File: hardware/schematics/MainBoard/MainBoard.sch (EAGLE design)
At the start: 16 parts, among them J1 T2M-105-01-X-D-TH-WT

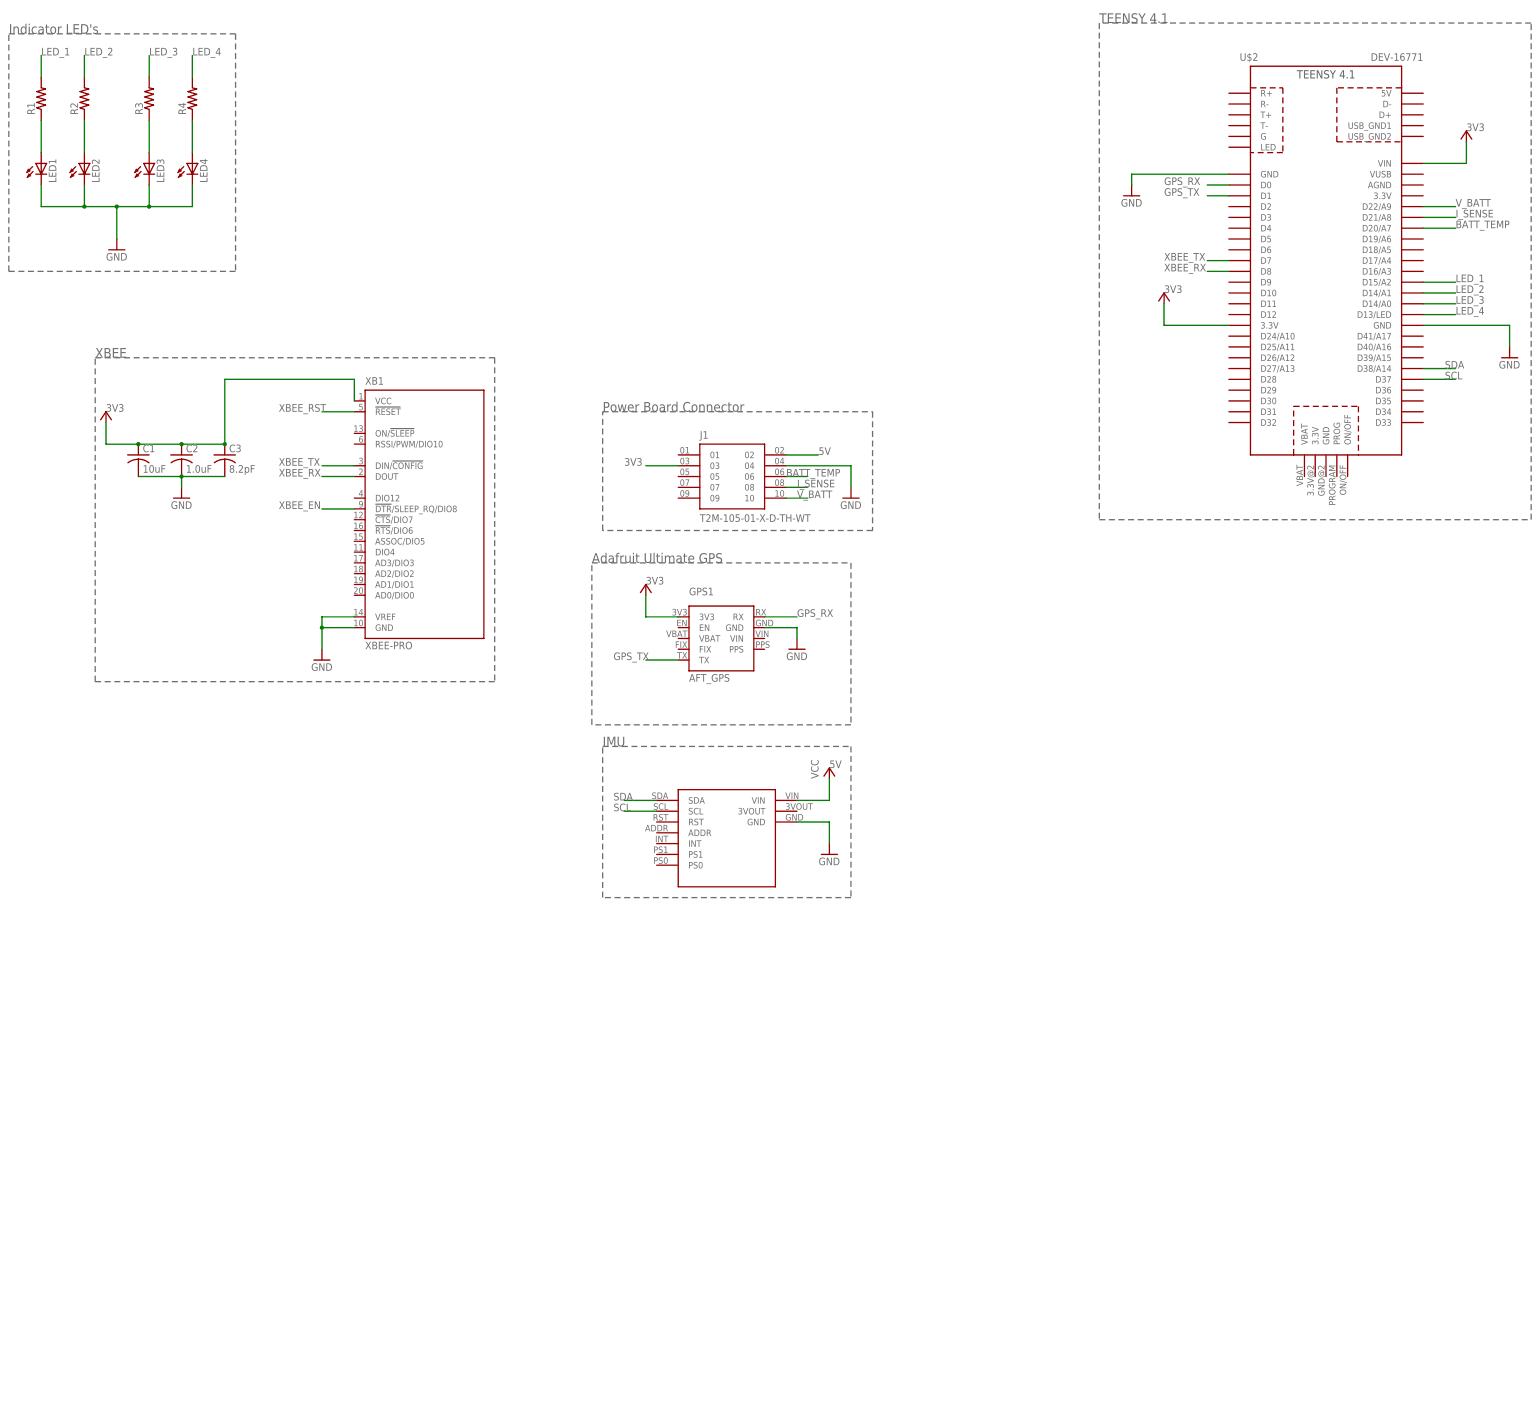
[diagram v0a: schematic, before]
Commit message: Added BMP388 & PDF's
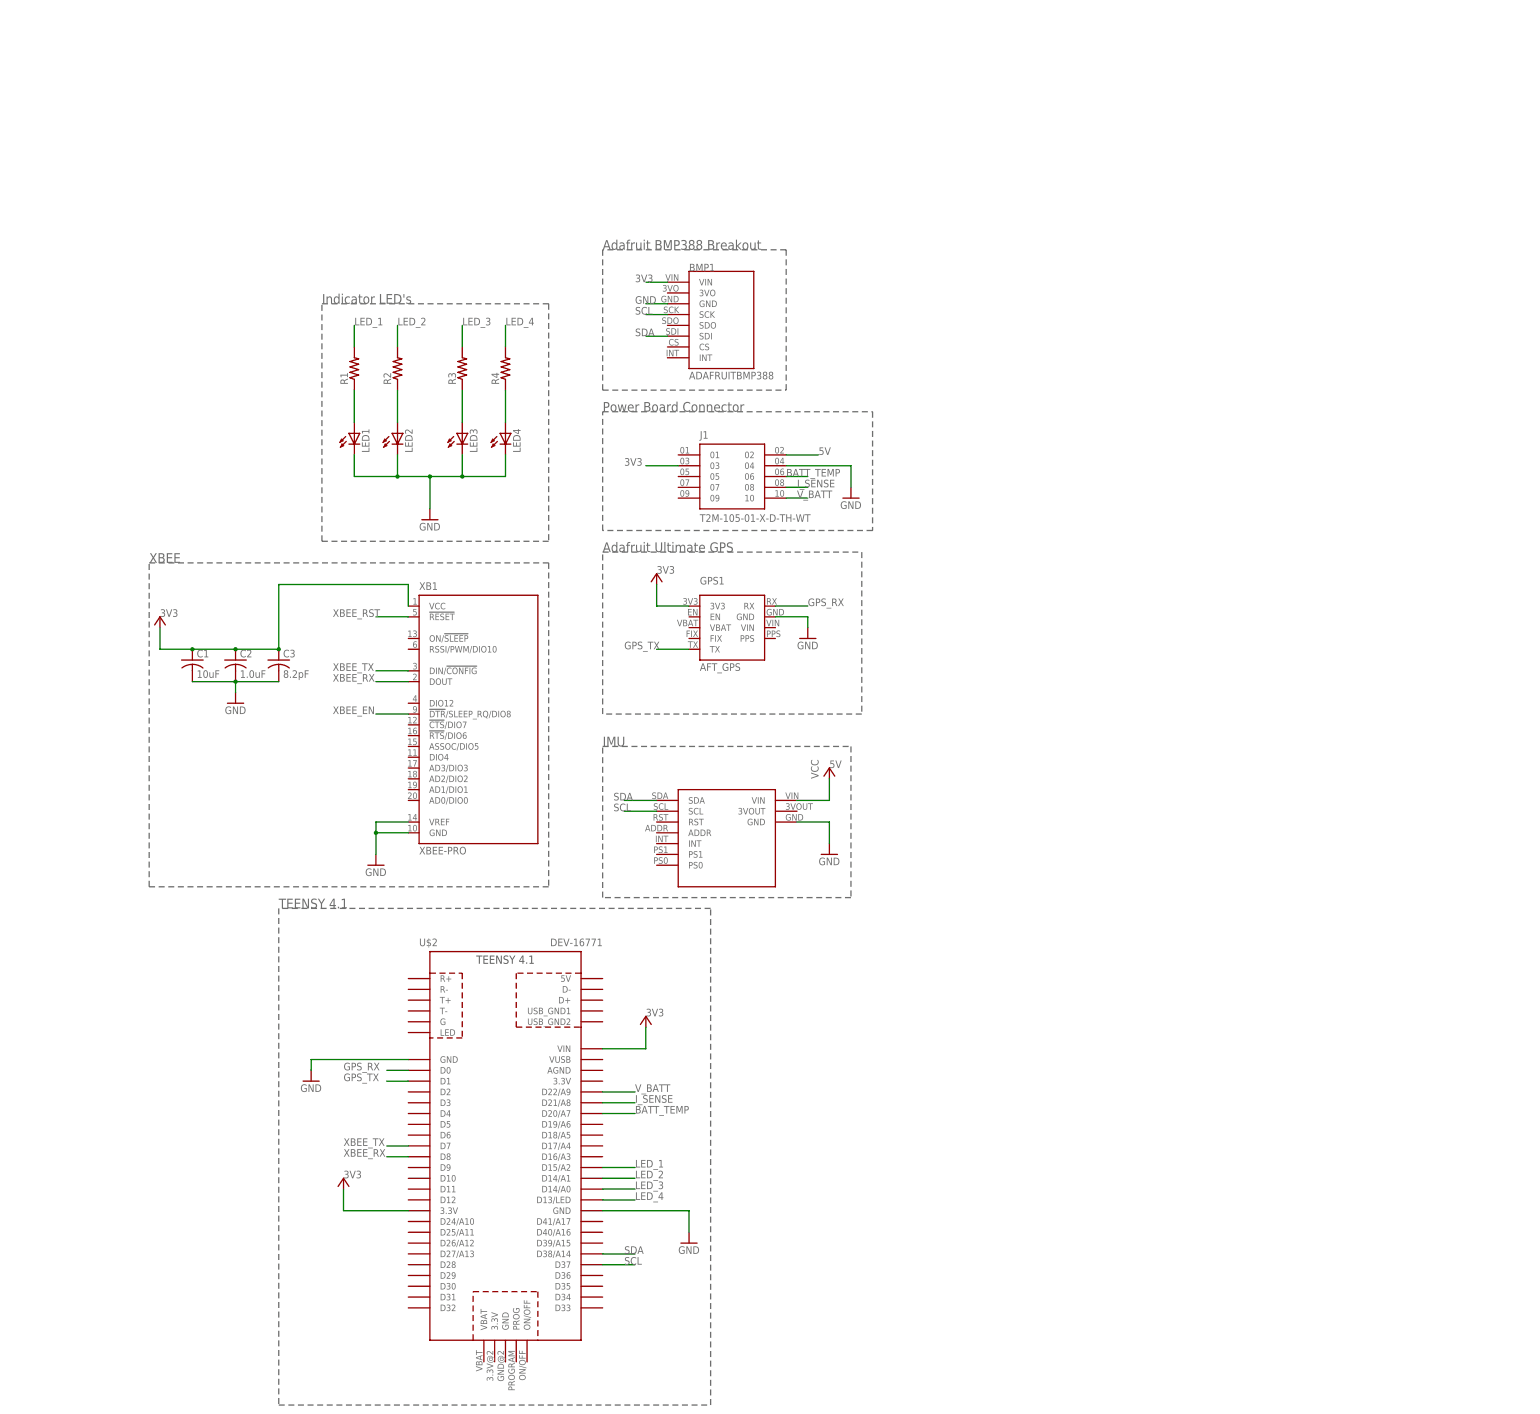
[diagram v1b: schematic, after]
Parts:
- added BMP1: ADAFRUITBMP388, adafruit BMP388:ADAFRUITBMP388
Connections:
- net 3V3: now also BMP1.VIN
- net GND: now also BMP1.GND
- net SCL: now also BMP1.SCK
- net SDA: now also BMP1.SDI
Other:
- note added: "Adafruit BMP388 Breakout"
- moved on the sheet: C1, C2, C3, GPS1, LED1, LED2, LED3, LED4, R1, R2, R3, R4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

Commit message: Added render image
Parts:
- renumbered J1 to SAMTEC_CONNECTOR
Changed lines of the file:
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@@
 <part name="R4" library="adafruit(seeIMUBreakout)" deviceset="R-US_" device="R0805"/>
 <part name="GND8" library="supply1" library_urn="urn:adsk.eagle:library:371" deviceset="GND" device=""/>
-<part name="J1" library="T2M-105-01-X-D-TH-WT" deviceset="T2M-105-01-X-D-TH-WT" device=""/>
+<part name="SAMTEC_CONNECTOR" library="T2M-105-01-X-D-TH-WT" deviceset="T2M-105-01-X-D-TH-WT" device=""/>
 <part name="GND7" library="supply1" library_urn="urn:adsk.eagle:library:371" deviceset="GND" device=""/>
 <part name="XB1" library="xbee" deviceset="XBEE" device="-PRO"/>
@@
 <attribute name="VALUE" x="30.48" y="30.48" size="1.778" layer="96"/>
 </instance>
-<instance part="J1" gate="G$1" x="104.14" y="43.18" smashed="yes">
+<instance part="SAMTEC_CONNECTOR" gate="G$1" x="104.14" y="43.18" smashed="yes">
 <attribute name="NAME" x="96.52" y="52.07" size="1.778" layer="95"/>
 <attribute name="VALUE" x="96.52" y="34.29" size="1.778" layer="96" align="top-left"/>
@@
 </segment>
 <segment>
-<pinref part="J1" gate="G$1" pin="03"/>
+<pinref part="SAMTEC_CONNECTOR" gate="G$1" pin="03"/>
 <wire x1="91.44" y1="45.72" x2="83.82" y2="45.72" width="0.1524" layer="91"/>
 <label x="78.74" y="45.72" size="1.778" layer="95"/>
@@
 </segment>
 <segment>
-<pinref part="J1" gate="G$1" pin="04"/>
+<pinref part="SAMTEC_CONNECTOR" gate="G$1" pin="04"/>
 <wire x1="116.84" y1="45.72" x2="132.08" y2="45.72" width="0.1524" layer="91"/>
 <wire x1="132.08" y1="45.72" x2="132.08" y2="40.64" width="0.1524" layer="91"/>
@@
 <net name="5V" class="0">
 <segment>
-<pinref part="J1" gate="G$1" pin="02"/>
+<pinref part="SAMTEC_CONNECTOR" gate="G$1" pin="02"/>
 <wire x1="116.84" y1="48.26" x2="124.46" y2="48.26" width="0.1524" layer="91"/>
 <label x="124.46" y="48.26" size="1.778" layer="95"/>
@@
 </segment>
 <segment>
-<pinref part="J1" gate="G$1" pin="10"/>
+<pinref part="SAMTEC_CONNECTOR" gate="G$1" pin="10"/>
 <wire x1="116.84" y1="38.1" x2="121.92" y2="38.1" width="0.1524" layer="91"/>
 <label x="119.38" y="38.1" size="1.778" layer="95"/>
@@
 </segment>
 <segment>
-<pinref part="J1" gate="G$1" pin="08"/>
+<pinref part="SAMTEC_CONNECTOR" gate="G$1" pin="08"/>
 <wire x1="116.84" y1="40.64" x2="121.92" y2="40.64" width="0.1524" layer="91"/>
 <label x="119.38" y="40.64" size="1.778" layer="95"/>
@@
 </segment>
 <segment>
-<pinref part="J1" gate="G$1" pin="06"/>
+<pinref part="SAMTEC_CONNECTOR" gate="G$1" pin="06"/>
 <wire x1="116.84" y1="43.18" x2="121.92" y2="43.18" width="0.1524" layer="91"/>
 <label x="116.84" y="43.18" size="1.778" layer="95"/>

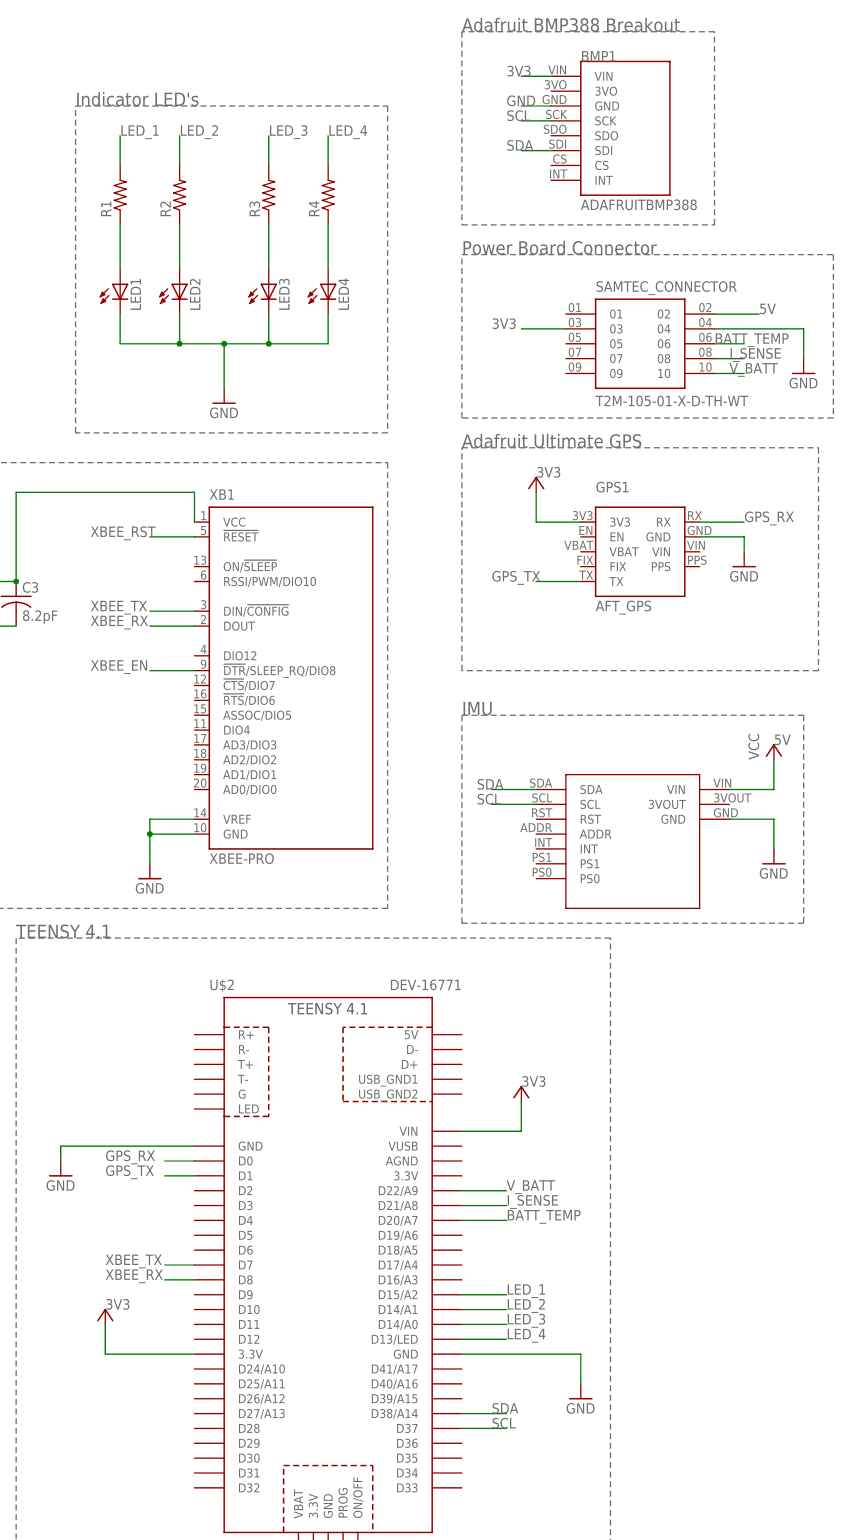
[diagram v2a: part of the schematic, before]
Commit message: Updates
Made power traces wider
Added XBEE enable and reset traces
Moved I2C pins to correct pins on teensy
Made caps 805 size
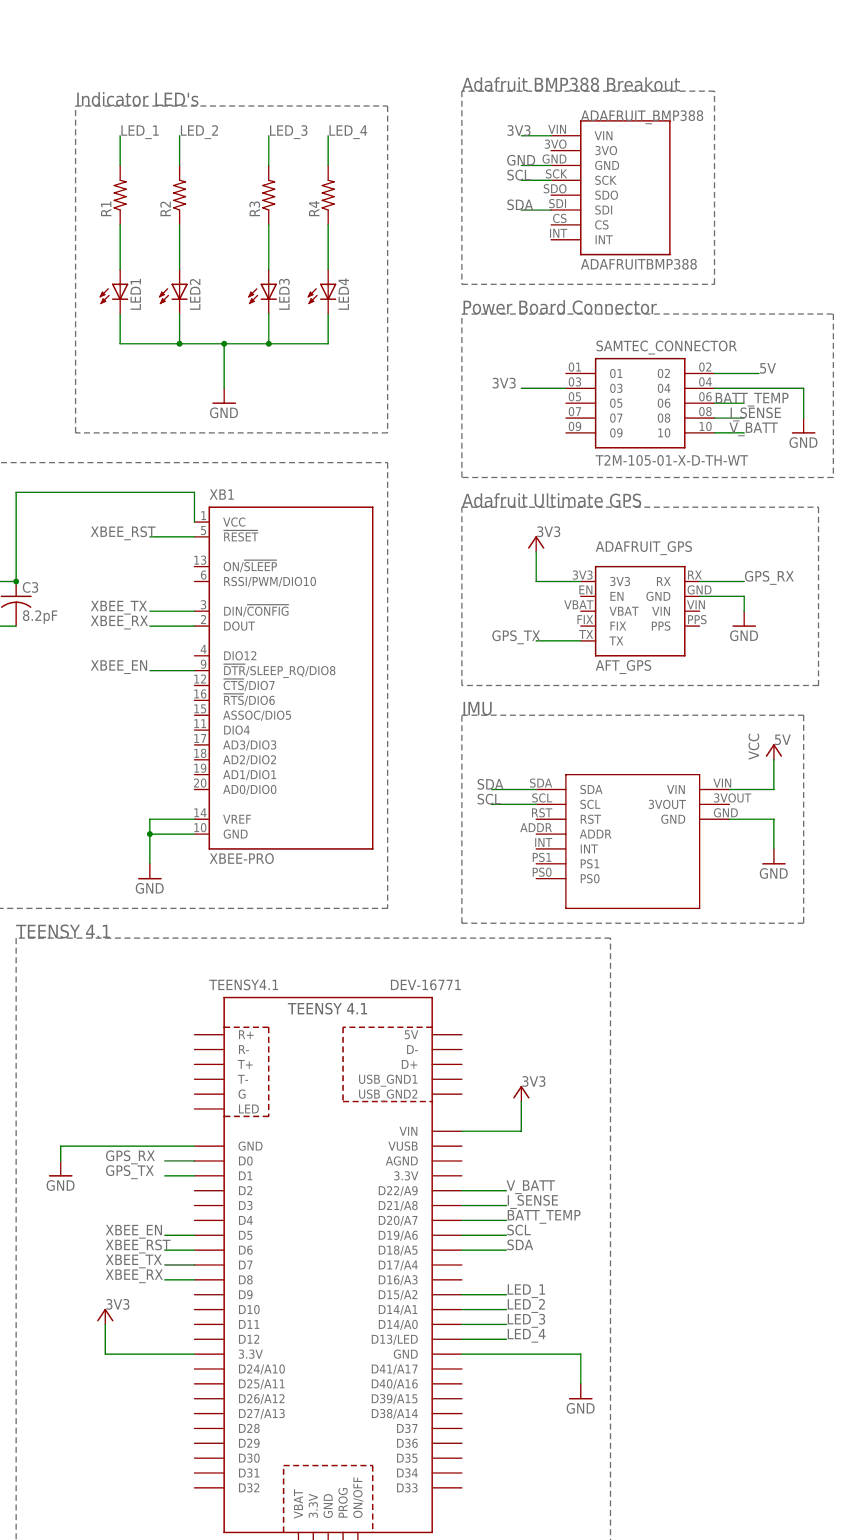
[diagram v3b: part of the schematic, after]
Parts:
- removed BMP1: ADAFRUITBMP388, adafruit BMP388:ADAFRUITBMP388
- removed GPS1: AFT_GPS, adafruit_Ultimate_GPS_Breakout:AFT_GPS
- added ADAFRUIT_BMP388: ADAFRUITBMP388, adafruit BMP388:ADAFRUITBMP388
- added ADAFRUIT_GPS: AFT_GPS, adafruit_Ultimate_GPS_Breakout:AFT_GPS
- renumbered U$2 to TEENSY4.1
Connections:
- net 3V3: now also ADAFRUIT_BMP388.VIN, ADAFRUIT_GPS.3V3; no longer BMP1.VIN, GPS1.3V3
- net GND: now also ADAFRUIT_BMP388.GND, ADAFRUIT_GPS.GND; no longer BMP1.GND, GPS1.GND
- net GPS_RX: now also ADAFRUIT_GPS.RX; no longer GPS1.RX
- net GPS_TX: now also ADAFRUIT_GPS.TX; no longer GPS1.TX
- net SCL: now also ADAFRUIT_BMP388.SCK, TEENSY4.1.D19/A6; no longer BMP1.SCK, TEENSY4.1.D37
- net SDA: now also ADAFRUIT_BMP388.SDI, TEENSY4.1.D18/A5; no longer BMP1.SDI, TEENSY4.1.D38/A14
- net XBEE_EN: now also TEENSY4.1.D5
- net XBEE_RST: now also TEENSY4.1.D6
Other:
- moved on the sheet: SAMTEC_CONNECTOR
